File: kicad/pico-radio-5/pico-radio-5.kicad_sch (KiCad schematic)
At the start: 6 parts, among them U1 SI4732-A10-GS, U2 TFT_320x240, U3 KY-040, Y1 Crystal

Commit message: Refactor code structure for improved readability and maintainability
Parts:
- added C1, C2: 22p, Capacitor_THT:C_Disc_D3.0mm_W1.6mm_P2.50mm, symbol Device:C
- added C3: 100nF, Capacitor_THT:C_Disc_D7.0mm_W2.5mm_P5.00mm, symbol Device:C
- added R1: R, Resistor_THT:R_Axial_DIN0207_L6.3mm_D2.5mm_P10.16mm_Horizontal, symbol Device:R
- added R2: R, symbol Device:R
- added R3, R4, R5, R6: 4.7k, Resistor_THT:R_Axial_DIN0207_L6.3mm_D2.5mm_P10.16mm_Horizontal, symbol Device:R
- Y1: value Crystal -> 32.768kHz
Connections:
- net +3.3V: now also R5.2
- net GND: now also C1.2, C2.1, R2.2, R6.1
- net VBUS_ATT: now reaches A1.32 (GPIO27_ADC1)
- net VBUS_ATT: now also R1.2, R2.1
- net +BATT: now reaches A1.40 (VBUS)
- net +BATT: now also R1.1
- net at U1.2 (GPO3/DCLK), Y1.1: now also C1.1
- net at U1.13 (RCLK), Y1.2: now also C2.2
- net AD_AUDIO renamed AD_FFT_AUDIO
- net AD_FFT_AUDIO: now also C3.2, R5.1, R6.2
- new net: C3.1, R3.2, R4.2
- new net AUDIO_L: R3.1
- new net AUDIO_R: R4.1
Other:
- moved on the sheet: Y1

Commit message: Refactor code structure for improved readability and maintainability
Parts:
- added BT1: BK-18650-PC2, Battery:BatteryHolder_MPD_BK-18650-PC2, symbol Device:BK-18650-PC2
- added C4, C5, C7: 4.7uF, Capacitor_THT:CP_Radial_D5.0mm_P2.50mm, symbol Device:C_Polarized
- added C6: 100nF, Capacitor_THT:C_Disc_D7.0mm_W2.5mm_P5.00mm, symbol Device:C
- added J1: HF Amplifier, Connector:NS-Tech_Grove_1x04_P2mm_Vertical, symbol Connector:Conn_01x04_Pin
- added Q1, Q2: PN2222A, Package_TO_SOT_THT:TO-92_Inline, symbol Transistor_BJT:PN2222A
- added R10, R7, R8, R9: 4.7k, Resistor_THT:R_Axial_DIN0207_L6.3mm_D2.5mm_P10.16mm_Horizontal, symbol Device:R
- added SW1: Reset, Button_Switch_SMD:SW_SPST_Omron_B3FS-100xP, symbol Switch:SW_Omron_B3FS
- R1: value R -> 200k
- R2: value R -> 100k
- R3, R4: value 4.7k -> 22k
- R5, R6: value 4.7k -> 10k
- Y1: value 32.768kHz -> 32.762kHz; footprint (none) -> Crystal:Crystal_C38-LF_D3.0mm_L8.0mm_Horizontal
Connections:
- net +BATT: now also J1.1 (Pin_1); no longer A1.40 (VBUS)
- net AUDIO_L: now also R4.1, C5.2, J1.3 (Pin_3), Q2.3 (C), R10.2; no longer R3.1
- net AUDIO_MUTE: now also R7.1, R8.1
- net AUDIO_R: now also R3.1, C4.2, J1.2 (Pin_2), Q1.3 (C), R9.2; no longer R4.1
- net GND: now also BT1.-, C6.2, C7.2, J1.4 (Pin_4), Q1.1 (E), Q2.1 (E), R10.1, R9.1, SW1.1
- net at A1.30 (RUN): now also SW1.2
- net +Vsys: now reaches A1.39 (VSYS)
- net at U1.1 (LOUT/DFS): now also C5.1
- net at U1.16 (ROUT/DOUT): now also C4.1
- net VBUS_ATT: no longer names the net of A1.32 (GPIO27_ADC1), R1.2, R2.1
- new net: Q1.2 (B), R7.2
- new net: Q2.2 (B), R8.2
- new net +Vbus: A1.40 (VBUS), BT1.+, C6.1, C7.1
- no-connect marks 14 -> 13
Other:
- title: (none) -> Pico radio-5
- moved on the sheet: A1, BZ1, C1, C2, C3, R1, R2, R3, R4, R5, R6, U1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

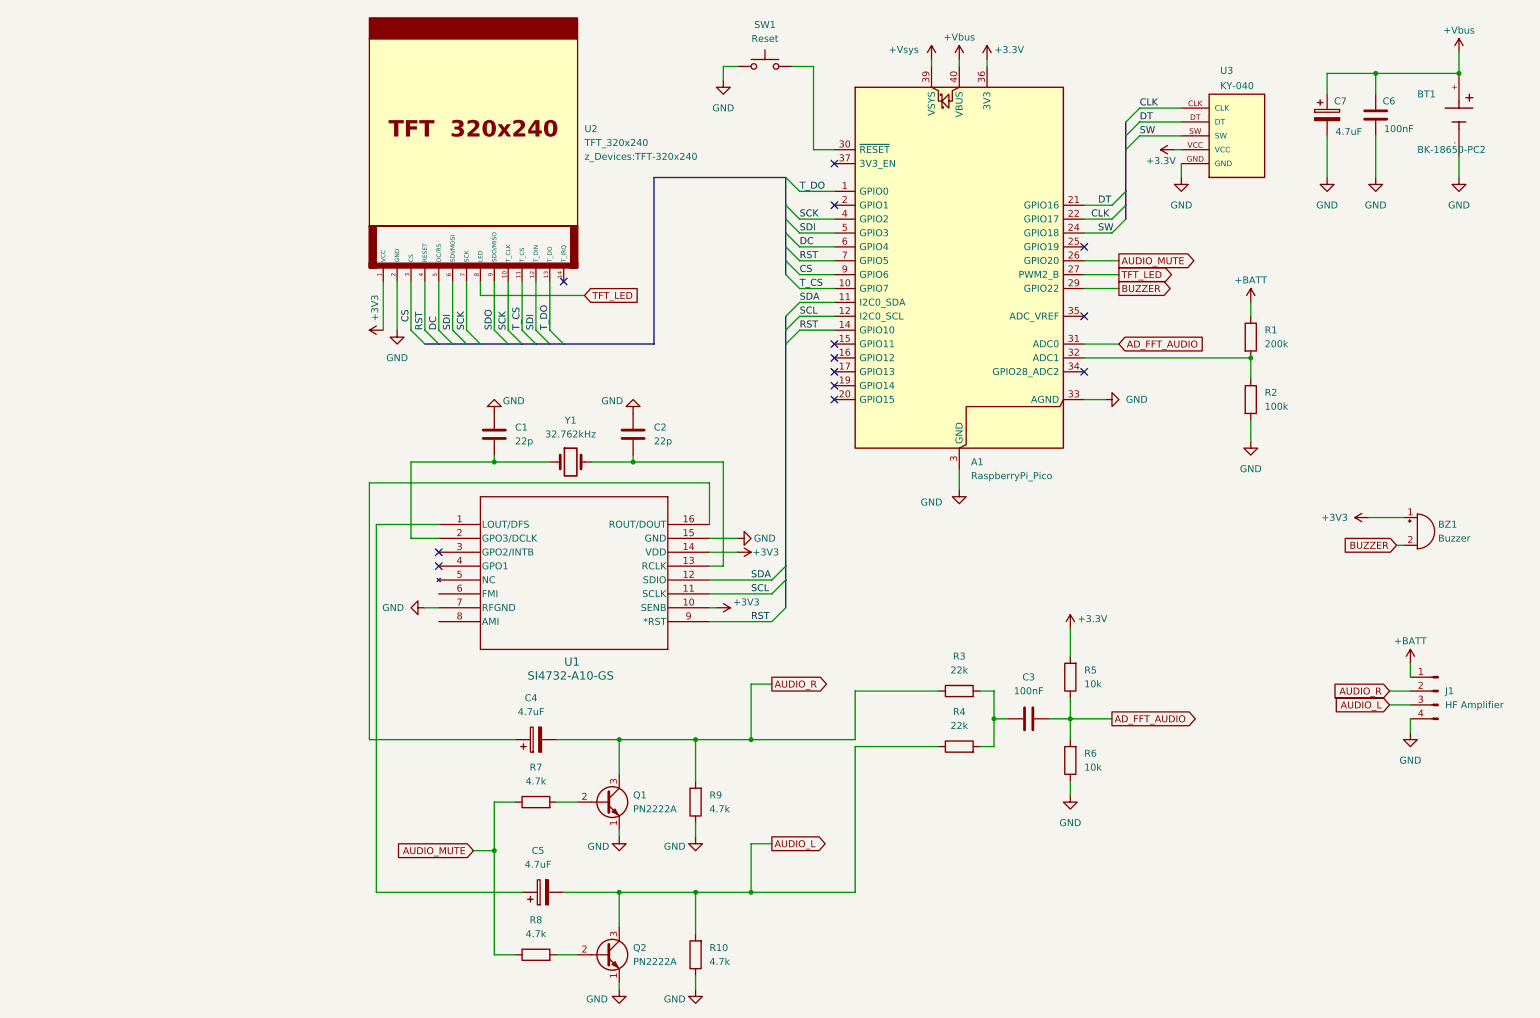
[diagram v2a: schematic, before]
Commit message: Add lock files for PCB and schematic of pico-radio-5 project
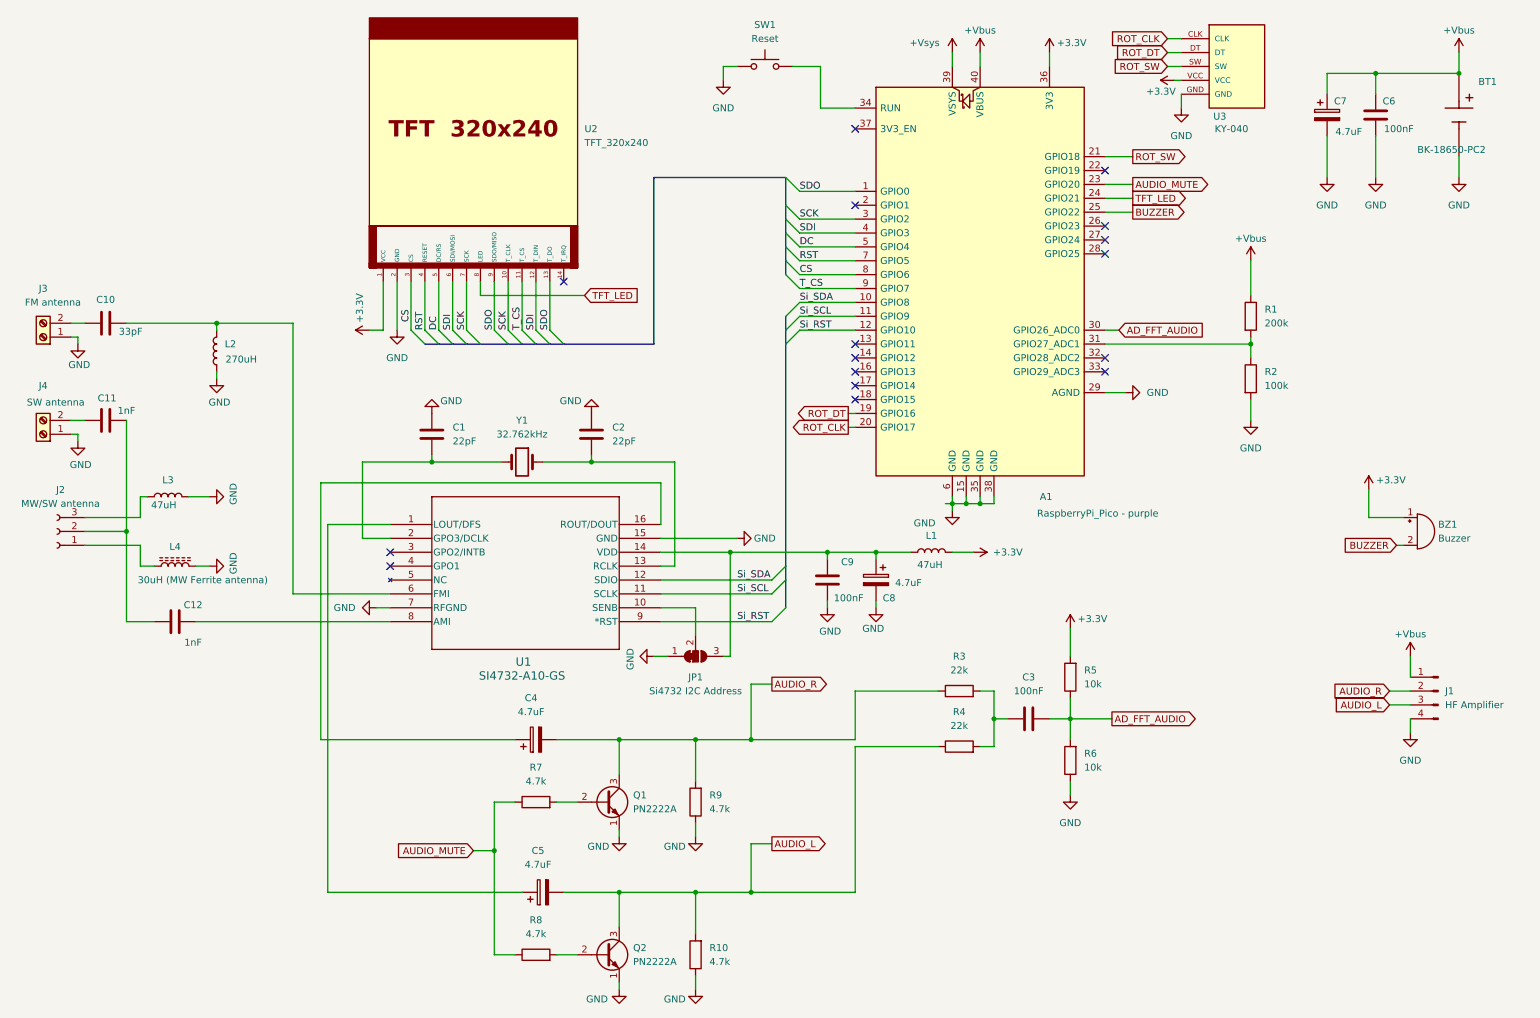
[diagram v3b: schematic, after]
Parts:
- added C10: 33pF, Capacitor_THT:C_Disc_D3.0mm_W1.6mm_P2.50mm, symbol Device:C
- added C11, C12: 1nF, Capacitor_THT:C_Disc_D3.0mm_W1.6mm_P2.50mm, symbol Device:C
- added C8: 4.7uF, Capacitor_THT:CP_Radial_D5.0mm_P2.50mm, symbol Device:C_Polarized
- added C9: 100nF, Capacitor_THT:C_Disc_D7.0mm_W2.5mm_P5.00mm, symbol Device:C
- added J2: MW/SW antenna, Connector_PinHeader_2.54mm:PinHeader_1x03_P2.54mm_Vertical, symbol Connector:Conn_01x03_Socket
- added J3: FM antenna, TerminalBlock_4Ucon:TerminalBlock_4Ucon_1x02_P3.50mm_Horizontal, symbol Connector:Screw_Terminal_01x02
- added J4: SW antenna, TerminalBlock_4Ucon:TerminalBlock_4Ucon_1x02_P3.50mm_Horizontal, symbol Connector:Screw_Terminal_01x02
- added JP1: Si4732 I2C Address, Jumper:SolderJumper-3_P1.3mm_Bridged12_RoundedPad1.0x1.5mm, symbol Jumper:SolderJumper_3_Bridged12
- added L1, L3: 47uH, Resistor_THT:R_Axial_DIN0207_L6.3mm_D2.5mm_P10.16mm_Horizontal, symbol Device:L
- added L2: 270uH, Resistor_THT:R_Axial_DIN0207_L6.3mm_D2.5mm_P10.16mm_Horizontal, symbol Device:L
- added L4: 30uH (MW Ferrite antenna), Connector_PinHeader_2.54mm:PinHeader_1x02_P2.54mm_Vertical, symbol Device:L_Ferrite
- A1: value RaspberryPi_Pico -> RaspberryPi_Pico - purple
- BZ1: footprint (none) -> Buzzer_Beeper:Buzzer_12x9.5RM7.6
- C1, C2: value 22p -> 22pF
- J1: footprint Connector:NS-Tech_Grove_1x04_P2mm_Vertical -> Connector_PinHeader_2.54mm:PinHeader_1x04_P2.54mm_Vertical
- R2: footprint (none) -> Resistor_THT:R_Axial_DIN0207_L6.3mm_D2.5mm_P10.16mm_Horizontal
- SW1: footprint Button_Switch_SMD:SW_SPST_Omron_B3FS-100xP -> Connector_PinHeader_2.54mm:PinHeader_1x02_P2.54mm_Vertical
- U1: footprint SOIC_A10-GS_SIL -> Package_SO:SOIC_A10-GS_SIL
- U2: footprint z_Devices:TFT-320x240 -> Connector_PinHeader_2.54mm:PinHeader_1x14_P2.54mm_Vertical
- U3: footprint KY-040:KY-040-PORT -> Rotary_Encoder:KY-040-PORT
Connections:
- net +BATT is gone; now on net +Vbus: J1.1 (Pin_1), R1.1
- net T_DO is gone; now on net SDO: A1.1 (GPIO0), U2.13 (T_DO)
- net +3.3V: now also BZ1.1 (+), U2.1 (VCC), L1.2
- net AD_FFT_AUDIO: now also A1.30 (GPIO26_ADC0); no longer A1.31 (GPIO26_ADC0)
- net AUDIO_MUTE: now also A1.23 (GPIO20); no longer A1.26 (GPIO20)
- net BUZZER: now also A1.25 (GPIO22); no longer A1.29 (GPIO22)
- net CS: now also A1.8 (GPIO6); no longer A1.9 (GPIO6)
- net DC: now also A1.5 (GPIO4); no longer A1.6 (GPIO4)
- net GND: now also A1.15 (GND), A1.29 (AGND), A1.35 (GND), A1.6 (GND), C8.2, C9.1, J3.1 (Pin_1), J4.1 (Pin_1), JP1.1 (A), L2.1, L3.2, L4.2; no longer A1.13 (GND), A1.18 (GND), A1.23 (GND), A1.28 (GND), A1.3 (GND), A1.33 (AGND), A1.8 (GND)
- net RST: no longer A1.14 (GPIO10), U1.9 (*RST)
- net SCK: now also A1.3 (GPIO2); no longer A1.4 (GPIO2)
- net SDI: now also A1.4 (GPIO3); no longer A1.5 (GPIO3)
- net TFT_LED: now also A1.24 (GPIO21); no longer A1.27 (GPIO21)
- net T_CS: now also A1.9 (GPIO7); no longer A1.10 (GPIO7)
- net at C1.1, U1.2 (GPO3/DCLK): now also Y1.2; no longer Y1.1
- net at SW1.2: now also A1.34 (RUN); no longer A1.30 (RUN)
- net at R1.2, R2.1: now also A1.31 (GPIO27_ADC1); no longer A1.32 (GPIO27_ADC1)
- net ROT_DT: now reaches A1.19 (GPIO16)
- net ROT_DT: now also U3.DT
- net ROT_CLK: now reaches A1.20 (GPIO17)
- net ROT_CLK: now also U3.CLK
- net at C2.2, U1.13 (RCLK): now also Y1.1; no longer Y1.2
- net at U1.6 (FMI): now also C10.1, L2.2
- net at U1.8 (AMI): now also C12.1
- removed net +3V3: BZ1.1 (+), U1.10 (SENB), U1.14 (VDD), U2.1 (VCC)
- net CLK: no longer names the net of A1.22 (GPIO19)
- net CLK: no longer U3.CLK
- net DT renamed ROT_SW
- net ROT_SW: now also U3.SW; no longer U3.DT
- net SCL renamed Si_RST
- net Si_RST: now also U1.9 (*RST); no longer U1.11 (SCLK)
- net SDA renamed Si_SCL
- net Si_SCL: now also U1.11 (SCLK); no longer U1.12 (SDIO)
- removed net SW: A1.24 (GPIO18), U3.SW
- new net: J2.1 (Pin_1), L4.1
- new net: C11.2, C12.2, J2.2 (Pin_2)
- new net: J2.3 (Pin_3), L3.1
- new net: C11.1, J4.2 (Pin_2)
- new net: C8.1, C9.2, JP1.3 (B), L1.1, U1.14 (VDD)
- new net: C10.2, J3.2 (Pin_2)
- new net: JP1.2 (C), U1.10 (SENB)
- new net Si_SDA: A1.10 (GPIO8), U1.12 (SDIO)
- no-connect marks 13 -> 16
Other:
- moved on the sheet: C1, C2, R1, U1, Y1

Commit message: Refactor code structure for improved readability and maintainability
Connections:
- net AUDIO_MUTE: now also A1.22 (GPIO19); no longer A1.23 (GPIO20)
- net BUZZER: now also A1.23 (GPIO20); no longer A1.25 (GPIO22)
- net LED: now reaches A1.2 (GPIO1)
- net LED: now also U2.8 (LED)
- net TFT_LED: no longer names the net of A1.24 (GPIO21)
- net TFT_LED: no longer U2.8 (LED)

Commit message: Refactor code structure for improved readability and maintainability
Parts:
- added JP2: NYÁK átkötés, R_Axial_DIN0207_L6.3mm_D2.5mm_P7.62mm_Horizontal, symbol Jumper:Jumper_2_Small_Bridged
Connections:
- net +Vbus: now also JP2.2 (B); no longer J1.1 (Pin_1)
- new net: J1.1 (Pin_1), JP2.1 (A)
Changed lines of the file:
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@@
 	(wire
 		(pts
+			(xy 266.7 125.73) (xy 266.7 124.46)
+		)
+		(stroke
+			(width 0)
+			(type default)
+		)
+	)
+	(wire
+		(pts
 			(xy 142.24 130.81) (xy 142.24 111.76)
 		)
@@
 	)
 	(symbol
+		(lib_id "power:+BATT")
+		(at 266.7 124.46 0)
+		(unit 1)
+		(exclude_from_sim no)
+		(in_bom yes)
+		(on_board yes)
+		(dnp no)
+		(property "Reference" "#PWR040"
+			(at 266.7 128.27 0)
+			(effects
+				(font
+					(size 1.27 1.27)
+				)
+				(hide yes)
+			)
+		)
+		(property "Value" "+Vbus"
+			(at 266.7 120.396 0)
+			(effects
+				(font
+					(size 1.27 1.27)
+				)
+			)
+		)
+		(property "Footprint" ""
+			(at 266.7 124.46 0)
+			(effects
+				(font
+					(size 1.27 1.27)
+				)
+				(hide yes)
+			)
+		)
+		(property "Datasheet" ""
+			(at 266.7 124.46 0)
+			(effects
+				(font
+					(size 1.27 1.27)
+				)
+				(hide yes)
+			)
+		)
+		(property "Description" "Power symbol creates a global label with name \"+BATT\""
+			(at 266.7 124.46 0)
+			(effects
+				(font
+					(size 1.27 1.27)
+				)
+				(hide yes)
+			)
+		)
+		(pin "1"
+		)
+		(instances
+			(project "pico-radio-5"
+				(path "/b9640508-dcc6-4f6b-830f-c53a732dcb5b"
+					(reference "#PWR040")
+					(unit 1)
+				)
+			)
+		)
+	)
+	(symbol
 		(lib_id "Display_Graphic:TFT_320x240")
 		(at 95.25 59.69 0)
@@
 	)
 	(symbol
+		(lib_id "Jumper:Jumper_2_Small_Bridged")
+		(at 266.7 128.27 90)
+		(unit 1)
+		(exclude_from_sim no)
+		(in_bom yes)
+		(on_board yes)
+		(dnp no)
+		(property "Reference" "JP2"
+			(at 261.62 128.27 0)
+			(effects
+				(font
+					(size 1.27 1.27)
+				)
+			)
+		)
+		(property "Value" "NYÁK átkötés"
+			(at 264.668 128.016 0)
+			(effects
+				(font
+					(size 1.27 1.27)
+				)
+			)
+		)
+		(property "Footprint" "R_Axial_DIN0207_L6.3mm_D2.5mm_P7.62mm_Horizontal"
+			(at 266.7 128.27 0)
+			(effects
+				(font
+					(size 1.27 1.27)
+				)
+				(hide yes)
+			)
+		)
+		(property "Datasheet" "~"
+			(at 266.7 128.27 0)
+			(effects
+				(font
+					(size 1.27 1.27)
+				)
+				(hide yes)
+			)
+		)
+		(property "Description" "Jumper, 2-pole, small symbol, bridged"
+			(at 266.7 128.27 0)
+			(effects
+				(font
+					(size 1.27 1.27)
+				)
+				(hide yes)
+			)
+		)
+		(pin "1"
+		)
+		(pin "2"
+		)
+		(instances
+			(project "pico-radio-5"
+				(path "/b9640508-dcc6-4f6b-830f-c53a732dcb5b"
+					(reference "JP2")
+					(unit 1)
+				)
+			)
+		)
+	)
+	(symbol
 		(lib_id "power:GND")
 		(at 87.63 86.36 180)
@@
 					(unit 1)
 				)
-			)
-		)
-	)
-	(symbol
-		(lib_id "power:+BATT")
-		(at 266.7 130.81 0)
-		(unit 1)
-		(exclude_from_sim no)
-		(in_bom yes)
-		(on_board yes)
-		(dnp no)
-		(property "Reference" "#PWR031"
-			(at 266.7 134.62 0)
-			(effects
-				(font
-					(size 1.27 1.27)
-				)
-				(hide yes)
-			)
-		)
-		(property "Value" "+Vbus"
-			(at 266.7 126.746 0)
-			(effects
-				(font
-					(size 1.27 1.27)
-				)
-			)
-		)
-		(property "Footprint" ""
-			(at 266.7 130.81 0)
-			(effects
-				(font
-					(size 1.27 1.27)
-				)
-				(hide yes)
-			)
-		)
-		(property "Datasheet" ""
-			(at 266.7 130.81 0)
-			(effects
-				(font
-					(size 1.27 1.27)
-				)
-				(hide yes)
-			)
-		)
-		(property "Description" "Power symbol creates a global label with name \"+BATT\""
-			(at 266.7 130.81 0)
-			(effects
-				(font
-					(size 1.27 1.27)
-				)
-				(hide yes)
-			)
-		)
-		(pin "1"
-		)
-		(instances
-			(project "pico-radio-5"
-				(path "/b9640508-dcc6-4f6b-830f-c53a732dcb5b"
-					(reference "#PWR031")
-					(unit 1)
-				)

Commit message: Add lock file for pico-radio-5 schematic to prevent concurrent edits
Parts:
- A1: footprint Module:RaspberryPi_Pico_Common_Unspecified -> Module:RaspberryPi_Pico_Common_THT-simple
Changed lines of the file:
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@@
 			)
 		)
-		(property "Footprint" "Module:RaspberryPi_Pico_Common_Unspecified"
+		(property "Footprint" "Module:RaspberryPi_Pico_Common_THT-simple"
 			(at 187.96 107.95 0)
 			(effects

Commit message: Refactor code structure for improved readability and maintainability
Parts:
- removed BT1: BK-18650-PC2, Battery:BatteryHolder_MPD_BK-18650-PC2, symbol Device:BK-18650-PC2
- added J5: Batterry, Connector_PinHeader_2.54mm:PinHeader_1x02_P2.54mm_Vertical, symbol Connector:Conn_01x02_Socket
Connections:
- net +Vbus: now also J5.1 (Pin_1)
- net GND: now also J5.2 (Pin_2)

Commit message: Refactor code structure for improved readability and maintainability
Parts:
- added Q3: PN2222A, Package_TO_SOT_THT:TO-92_Inline, symbol Transistor_BJT:PN2222A
- added R11: 4.7k, Resistor_THT:R_Axial_DIN0207_L6.3mm_D2.5mm_P10.16mm_Horizontal, symbol Device:R
- JP2: footprint R_Axial_DIN0207_L6.3mm_D2.5mm_P7.62mm_Horizontal -> Resistor_THT:R_Axial_DIN0207_L6.3mm_D2.5mm_P10.16mm_Horizontal
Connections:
- net BUZZER: now also R11.1; no longer BZ1.2 (-)
- net GND: now also Q3.1 (E)
- new net: Q3.2 (B), R11.2
- new net: BZ1.2 (-), Q3.3 (C)
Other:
- moved on the sheet: BZ1
